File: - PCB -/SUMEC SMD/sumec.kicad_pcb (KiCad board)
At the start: 2 copper layers, 92 x 84 mm, 55 parts, among them IC1 XT30U-F, J1 Conn_01x04_Pin, J2 USB3090-XX-X_REVE, J3 Conn_01x06_Pin, J4 Conn_01x06_Pin, J5 Conn_01x06_Pin, J6 Conn_01x01_Pin, J7 Conn_01x01_Pin, Q1 PMOS, SW1 SW_SPDT, SW2 SW_Push, SW3 SW_Push, SW4 SW_Push, U1 TB6612FNG, U11 LM1084-3.3, U12 QRE1113, U13 QRE1113, U5 TSOP382xx, U6 QRE1113, U7 QRE1113, U9 ESP32-S3-WROOM-1

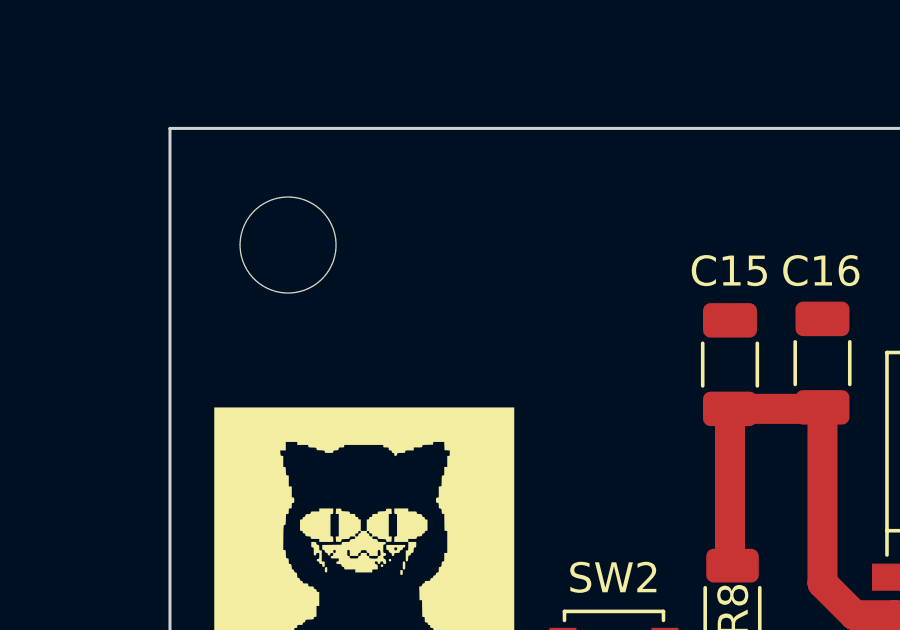
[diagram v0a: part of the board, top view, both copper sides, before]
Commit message: Fixed mission critical errror with smd pcb that savva couldn't fix
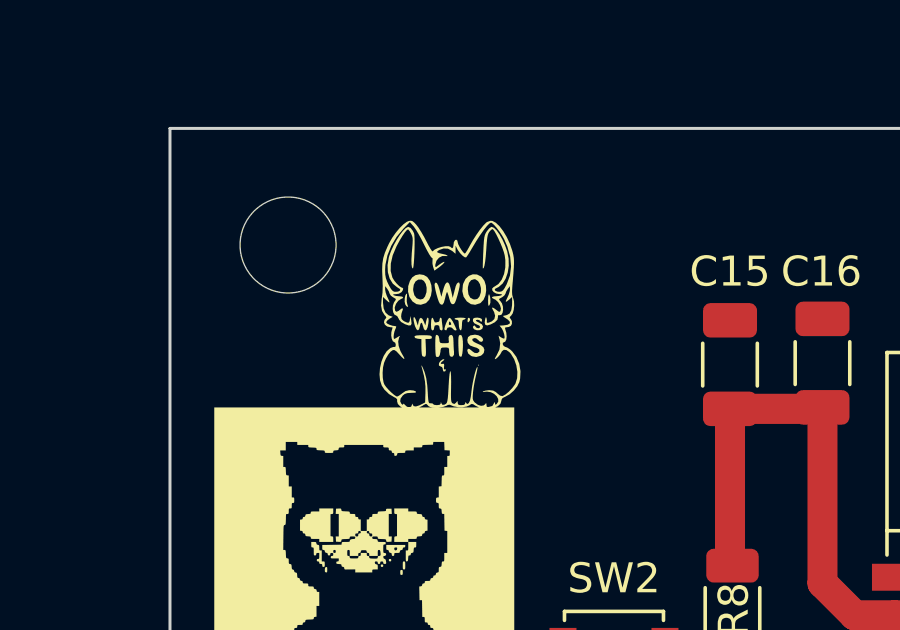
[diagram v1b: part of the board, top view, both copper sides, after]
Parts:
- added G***: LOGO, LOGO, F.Cu at (160.0, 50.7)

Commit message: pcb board update
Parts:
- removed G***: LOGO, LOGO
- removed J7: Conn_01x01_Pin, Connector_Wire:SolderWire-0.1sqmm_1x01_D0.4mm_OD1mm
- added J8: Conn_01x03_Pin, Connector_PinSocket_2.54mm:PinSocket_1x03_P2.54mm_Vertical, F.Cu at (186.8, 48.0)
- moved J3 88.6 mm to (178.1, 23.4)
- moved J4 88.6 mm to (153.6, 23.4)
- moved J5 88.6 mm to (166.2, 23.4)
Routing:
- net +3V3: track 302.4 -> 333.9 mm
- net QRE1113 A: track 2.44 -> 26.9 mm, vias 0 -> 1
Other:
- board text added: "maximalni mozni rozmer plosnaku scl sda - lasery (Univerzalni konektory)"
- board text added: "zadní čast plošnaku udělame to na pajivim pole nebo u knopa"
- board text removed: ":3"
- board text removed: "maximalni mozni rozmer plosnaku prokovy pres VIA nebo connector (solder wire) scl sda - lasery (Univerzalni konektory)"

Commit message: pcb board update
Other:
- board text added: ">:3"

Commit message: pcb scheamtic and board update
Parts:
- removed D2, D3, D4, D5: ESD5Zxx, Diode_SMD:D_SOD-523
- removed Q1: PMOS, Package_TO_SOT_SMD:SOT-223
- removed U6: QRE1113, sumec-smd_library:QRE1113GR-(smd)
- added C5: 100nF, Capacitor_SMD:C_1206_3216Metric, F.Cu at (206.0, 72.5)
- added R12: 0R, Resistor_SMD:R_1206_3216Metric, F.Cu at (275.5, 41.9)
- added R14: 0R, Resistor_SMD:R_1206_3216Metric, F.Cu at (275.5, 45.2)
- added R15: 0R, Resistor_SMD:R_1206_3216Metric, F.Cu at (275.5, 48.5)
- added R16: 0R, Resistor_SMD:R_1206_3216Metric, F.Cu at (275.5, 51.8)
- added R17: 0R, Resistor_SMD:R_1206_3216Metric, F.Cu at (275.5, 55.1)
- added R18: 0R, Resistor_SMD:R_1206_3216Metric, F.Cu at (275.5, 58.4)
- added R6: 0R, Resistor_SMD:R_1206_3216Metric, F.Cu at (200.4, 74.6)
- added U2: USBLC6-2SC6, Package_TO_SOT_SMD:TSOT-23-6_HandSoldering, F.Cu at (187.5, 76.0)
- C15: value 0,1uF.mcu -> 100nF.mcu
- C3: value 0,1uF.en -> 100nF.en
- C4: value 0,1uF.boot -> 100nF.boot
- C9: value 0,1uF.hbc -> 100nF.hbc
- J2: footprint sumec-smd_library:GCT_USB3090-XX-X_REVE -> Connector_USB:USB_C_Plug_Molex_105444
- R2: value 100 -> 15R; moved to F.Cu
- R3: value 10k -> 15R; moved to F.Cu
- moved D1 137.6 mm to (294.0, 42.0), turned to 0 degrees
- moved J4 132.8 mm to (283.8, 49.7), turned to 0 degrees
- moved J6 128.1 mm to (293.0, 47.5)
- moved J5 122.0 mm to (283.8, 55.9), turned to 0 degrees
- moved J3 107.5 mm to (283.8, 43.4), turned to 0 degrees
- moved C15 100.5 mm to (268.4, 69.6)
- moved C16 100.5 mm to (271.5, 69.6)
- moved C17 100.5 mm to (267.2, 83.7)
- moved C3 100.5 mm to (264.8, 83.7)
- moved R8 100.5 mm to (268.5, 77.8)
- moved SW2 100.5 mm to (264.6, 79.2)
- moved C10 96.0 mm to (242.5, 18.4)
- moved C7 96.0 mm to (243.2, 24.0)
- moved C8 96.0 mm to (245.0, 18.4)
- moved C9 96.0 mm to (247.6, 18.4)
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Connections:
- net +5V renamed VBUS 5V
- net /MCU/AI1 renamed AI1
- net /MCU/AI2 renamed AI2
- net /MCU/BI1 renamed BI1
- net /MCU/BI2 renamed BI2
- net /MCU/BOOT renamed BOOT
- net /MCU/EN renamed EN
- net /MCU/PWMA renamed PWMA
- net /MCU/PWMB renamed PWMB
- net /MCU/STBY renamed STBY
- net 8V IN renamed VBATT
- C8 pad 1: /MCU/VM -> +8V
- C9 pad 1: /MCU/VM -> +8V
- J3 pad 5: GND -> Net-(J3-Pin_5)
- J4 pad 5: GND -> Net-(J4-Pin_5)
- J5 pad 5: GND -> Net-(J5-Pin_5)
- R2 pad 2: +3V3 -> Net-(R2-Pad2)
- R3 pad 1: +3V3 -> Net-(J2-D-)
- R3 pad 2: QRE1113 A -> Net-(R3-Pad2)
- U1 pad 13: /MCU/VM -> +8V
- U1 pad 14: /MCU/VM -> +8V
- U1 pad 24: /MCU/VM -> +8V
- U9 pad 13: /MCU/D - -> D-
- U9 pad 14: /MCU/D + -> D+
- U9 pad 4: QRE1113 A -> unconnected-(U9-GPIO4/TOUCH4/ADC1_CH3-Pad4)
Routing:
- net +3V3: track 333.9 -> 6.33 mm, vias 3 -> 0
- net QRE1113 D: track 88.3 -> 0.00 mm, vias 3 -> 0
- net QRE1113 B: track 76.4 -> 0.00 mm, vias 3 -> 0
- net MOTOR 1 +: track 65.6 -> 0.00 mm
- net Net-(D7.hbc2-A): track 62.6 -> 0.00 mm, vias 2 -> 0
- net MOTOR 1 -: track 60.9 -> 0.00 mm
- net MOTOR 2 -: track 57.6 -> 0.00 mm
- net /MCU/VM: track 57.1 -> 0.00 mm, vias 2 -> 0
- net MOTOR 2 +: track 51.6 -> 0.00 mm
- net QRE1113 C: track 47.7 -> 0.00 mm, vias 3 -> 0
- net QRE1113 A: track 26.9 -> 0.00 mm, vias 1 -> 0
- net /MCU/D +: track 20.5 -> 0.00 mm
- net PWMA: track 20.3 -> 0.00 mm
- net TEST PROGRAM: track 20.3 -> 0.00 mm, vias 2 -> 0
- net /MCU/D -: track 20.2 -> 0.00 mm
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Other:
- board size 92 x 84 mm -> 92 x 56.5 mm
- board text removed: "zadní čast plošnaku udělame to na pajivim pole nebo u knopa"

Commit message: pcb  board layout
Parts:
- removed C10: 0,5uF.hbc, Capacitor_SMD:C_1206_3216Metric
- removed D7.hbc2: D_Zener, Diode_SMD:D_1206_3216Metric
- removed the R6 at (239.7, 23.8)
- removed the R6 at (200.4, 74.6)
- removed SW2: SW_Push, Button_Switch_SMD:SW_SPST_B3U-1000P
- added EN: SW_Push, Button_Switch_SMD:SW_SPST_B3U-1000P, F.Cu at (163.5, 88.8)
- added R6: 0R, Resistor_SMD:R_1206_3216Metric, B.Cu at (154.2, 76.8)
- C15, C16, C6, C7, C8, C9: moved to B.Cu
- J2: value USB3090-XX-X_REVE -> TYPE-C-31-M-12; footprint Connector_USB:USB_C_Plug_Molex_105444 -> sumec-smd_library:HRO_TYPE-C-31-M-12
- moved R7 141.1 mm to (250.0, 108.8)
- moved D1 137.4 mm to (161.8, 79.2), turned to 180 degrees
- moved J6 121.8 mm to (175.2, 78.5)
- moved C16 109.9 mm to (161.7, 74.2), turned to 0 degrees
- moved C15 106.9 mm to (161.7, 76.5), turned to 0 degrees
- moved C3 101.2 mm to (163.5, 85.8), turned to 180 degrees
- moved R8 100.1 mm to (168.7, 85.8), turned to 0 degrees
- moved C17 98.7 mm to (168.7, 88.2), turned to 180 degrees
- moved C4 80.3 mm to (176.5, 50.8)
- moved BOOT 79.9 mm to (176.7, 47.8)
- moved J3 78.1 mm to (215.8, 81.9)
- moved R15 76.8 mm to (208.0, 85.2), turned to 180 degrees
- moved R17 76.6 mm to (208.0, 91.2), turned to 180 degrees
- moved R14 75.4 mm to (208.0, 78.8), turned to 180 degrees
- moved J5 75.3 mm to (215.8, 88.2)
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- renumbered SW4 to BOOT, SW3 to TEST
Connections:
- J2 pad A5: (no net) -> unconnected-(J2-CC1-PadA5)
- J2 pad A6: (no net) -> D+ IN
- J2 pad A7: (no net) -> D- IN
- J2 pad A8: (no net) -> unconnected-(J2-SBU1-PadA8)
- J2 pad B5: (no net) -> unconnected-(J2-CC2-PadB5)
- J2 pad B8: (no net) -> unconnected-(J2-SBU2-PadB8)
- J2 pad S1: (no net) -> Net-(J2-SHIELD-PadS1)
- R2 pad 1: Net-(J2-D+) -> D+ IN
- R3 pad 1: Net-(J2-D-) -> D- IN
- U9 pad 33: unconnected-(U9-MTDO/GPIO40/CLK_OUT2-Pad33) -> X-SHUT3
- U9 pad 34: unconnected-(U9-MTDI/GPIO41/CLK_OUT1-Pad34) -> X-SHUT2
- U9 pad 35: unconnected-(U9-MTMS/GPIO42-Pad35) -> X-SHUT1
- U9 pad 4: unconnected-(U9-GPIO4/TOUCH4/ADC1_CH3-Pad4) -> QRE1113 A
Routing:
- net +8V: track 18.7 -> 12.4 mm, vias 0 -> 2
- net +3V3: track 6.33 -> 6.24 mm, vias 0 -> 1

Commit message: PCB board update
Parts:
- U12, U13, U7: footprint sumec-smd_library:QRE1113GR-(smd) -> sumec_library:OnSemi_CASE100AQ - QRE1113
- moved J3 18.5 mm to (197.5, 79.0)
- moved J4 18.5 mm to (197.5, 72.8)
- moved J5 18.5 mm to (197.5, 85.2)
- moved R12 18.5 mm to (205.2, 75.8)
- moved R14 18.5 mm to (189.8, 75.8)
- moved R15 18.5 mm to (189.8, 82.3)
- moved R16 18.5 mm to (205.2, 82.1)
- moved R17 18.5 mm to (189.8, 88.3)
- moved R18 18.5 mm to (205.2, 88.3)
- moved R10 2.88 mm to (158.2, 94.0)
- moved U12 2.14 mm to (239.0, 95.5)
- moved U13 2.14 mm to (156.0, 95.5)
- moved U7 2.14 mm to (197.5, 95.5)
- moved R6 1.53 mm to (152.8, 76.3), turned to 90 degrees
- moved R13 1.30 mm to (233.5, 98.0), turned to -90 degrees
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- renumbered EN to SW2, TEST to SW3, BOOT to SW4
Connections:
- U9 pad 19: unconnected-(U9-GPIO11/TOUCH11/ADC2_CH0/FSPID/FSPIIO5/SUBSPID-Pad19) -> PWMA
- U9 pad 24: PWMA -> unconnected-(U9-GPIO47/SPICLK_P/SUBSPICLK_P_DIFF-Pad24)
- U9 pad 33: X-SHUT3 -> X-SHUT1
- U9 pad 35: X-SHUT1 -> X-SHUT3
- U9 pad 5: QRE1113 B -> QRE1113 D
- U9 pad 7: QRE1113 D -> QRE1113 B
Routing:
- net +3V3: track 6.24 -> 275.6 mm, vias 1 -> 6
- net QRE1113 D: track 0.00 -> 94.8 mm, vias 0 -> 2
- net SCL: track 0.00 -> 57.1 mm, vias 0 -> 2
- net +8V: track 12.4 -> 67.6 mm, vias 2 -> 4
- net QRE1113 A: track 0.00 -> 52.4 mm, vias 0 -> 2
- net QRE1113 B: track 0.00 -> 49.6 mm, vias 0 -> 3
- net X-SHUT3: track 0.00 -> 49.5 mm, vias 0 -> 2
- net SDA: track 0.00 -> 46.3 mm, vias 0 -> 2
- net X-SHUT2: track 0.00 -> 43.0 mm, vias 0 -> 2
- net QRE1113 C: track 0.00 -> 38.3 mm, vias 0 -> 1
- net X-SHUT1: track 0.00 -> 36.0 mm, vias 0 -> 2
- net IR MODULE: track 0.00 -> 34.3 mm
- net GND: track 0.00 -> 30.5 mm, vias 0 -> 2
- net EN: track 0.00 -> 29.5 mm
- net VBUS 5V: track 0.00 -> 22.6 mm, vias 0 -> 2
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- removed copper zone on B.Cu, net GND

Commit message: pcb board update (tlacitka a qre/tht)
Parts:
- moved SW4 4.22 mm to (173.3, 50.2), turned to 0 degrees
- moved C4 3.20 mm to (178.8, 53.0), turned to -90 degrees
- moved SW3 1.98 mm to (161.2, 49.5), turned to -90 degrees
- moved U5 0.33 mm to (186.8, 55.8)
- moved J8 0.31 mm to (186.8, 51.0)
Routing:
- net +3V3: track 275.6 -> 279.1 mm
- net TEST PROGRAM: track 4.83 -> 1.99 mm
- net BOOT: track 5.28 -> 7.07 mm
- net QRE1113 A: track 52.4 -> 53.5 mm
- added copper zone on B.Cu, net GND

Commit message: pcb board cleanup
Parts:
- moved R7 67.4 mm to (210.0, 54.5)
- moved R1 12.7 mm to (216.4, 96.8)
- moved EN 0.05 mm to (163.6, 88.8)
- renumbered SW4 to BOOT, SW2 to EN, SW3 to TEST
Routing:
- net GND: track 30.5 -> 24.7 mm
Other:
- board text removed: "maximalni mozni rozmer plosnaku scl sda - lasery (Univerzalni konektory)"
